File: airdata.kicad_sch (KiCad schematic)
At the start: 5 parts, among them J1 AE-MICRO-SD-DIP, U1 DPS310, U2 SeeeduinoXIAO

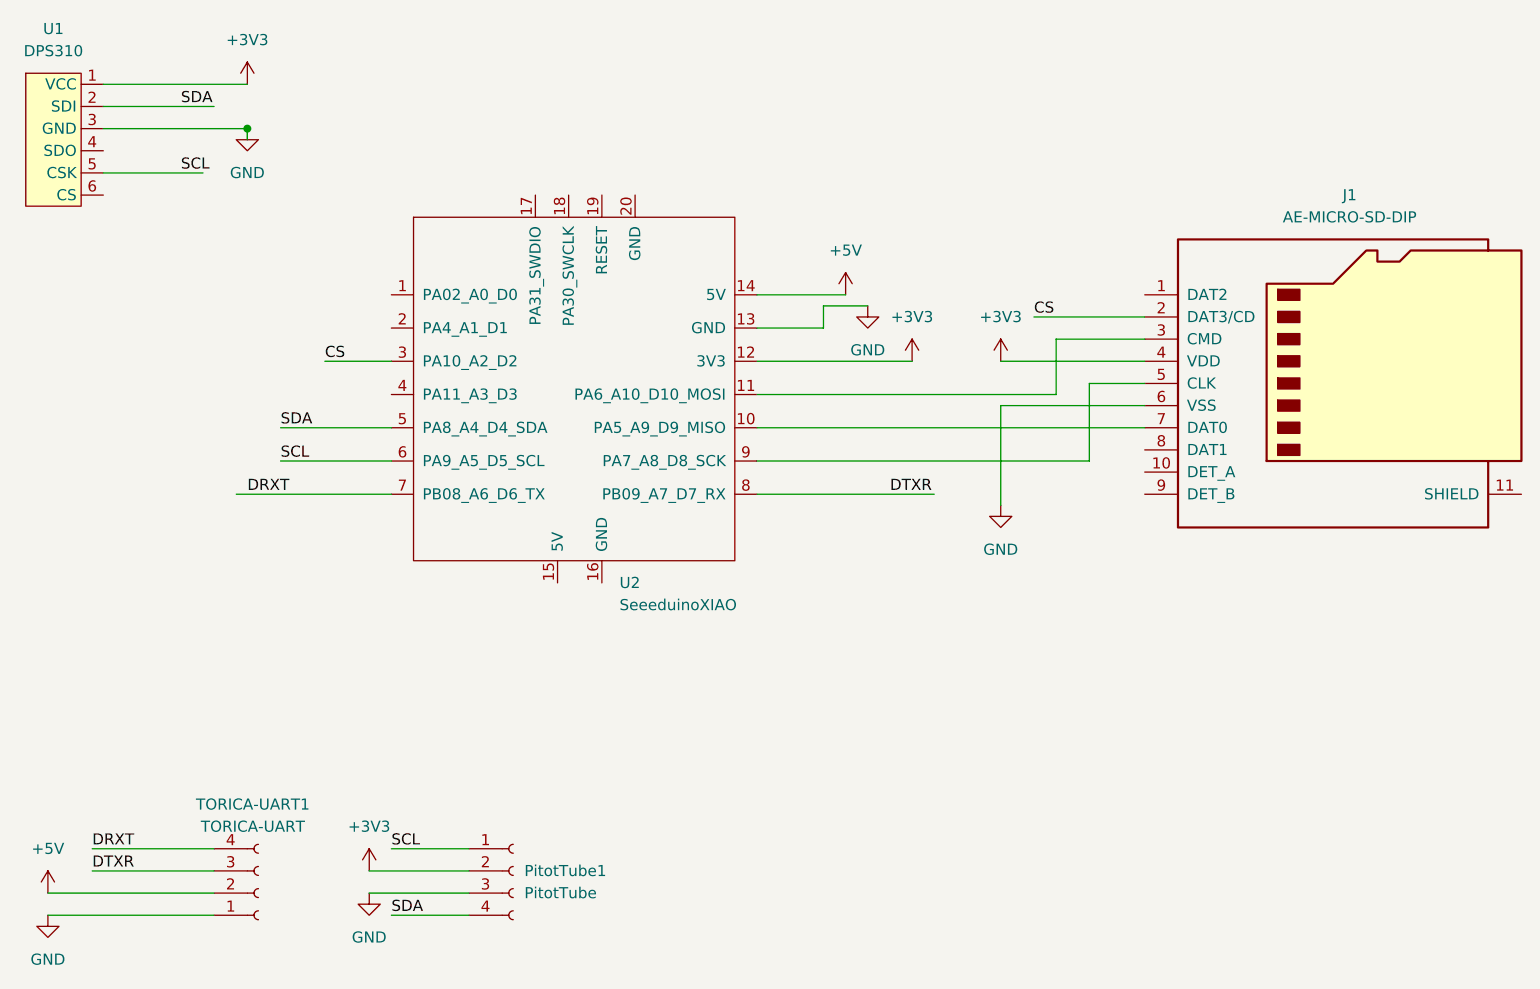
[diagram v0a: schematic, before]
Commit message: update to 24th add R
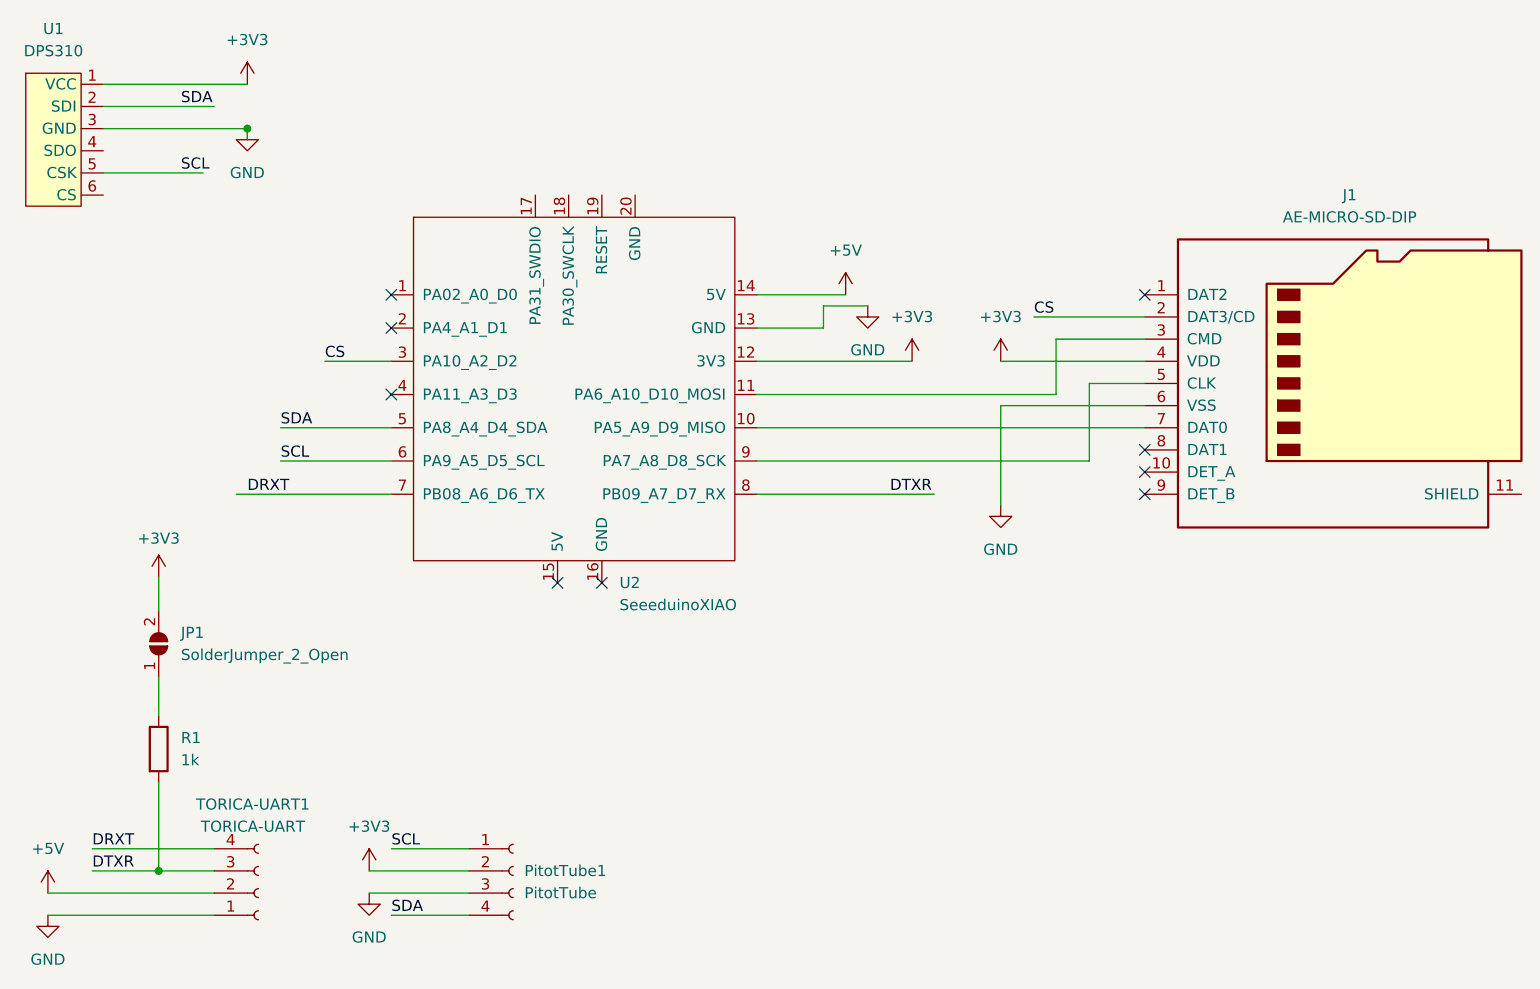
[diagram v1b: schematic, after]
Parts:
- added JP1: SolderJumper_2_Open, symbol Jumper:SolderJumper_2_Open
- added R1: 1k, symbol Device:R
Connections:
- net +3V3: now also JP1.2 (B)
- net DTXR: now also R1.2
- new net: JP1.1 (A), R1.1
- no-connect marks 0 -> 9
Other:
- company: (none) -> TORICA-24th
- title: (none) -> AirData

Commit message: Update PCB_Air
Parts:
- JP1: footprint (none) -> Jumper:SolderJumper-2_P1.3mm_Open_RoundedPad1.0x1.5mm
- R1: footprint (none) -> Resistor_THT:R_Axial_DIN0204_L3.6mm_D1.6mm_P7.62mm_Horizontal
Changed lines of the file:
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@@
       (effects (font (size 1.27 1.27)) (justify right))
     )
-    (property "Footprint" "" (at 33.02 86.995 0)
+    (property "Footprint" "Jumper:SolderJumper-2_P1.3mm_Open_RoundedPad1.0x1.5mm" (at 33.02 86.995 0)
       (effects (font (size 1.27 1.27)) hide)
     )
@@
       (effects (font (size 1.27 1.27)) (justify left))
     )
-    (property "Footprint" "" (at 31.242 99.06 90)
+    (property "Footprint" "Resistor_THT:R_Axial_DIN0204_L3.6mm_D1.6mm_P7.62mm_Horizontal" (at 31.242 99.06 90)
       (effects (font (size 1.27 1.27)) hide)
     )
